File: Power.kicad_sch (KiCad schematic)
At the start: 26 parts, among them J2 Jack-DC, J6 Jack-DC, Q1 AO3401A, Q2 AO3401A, SW1 SW_SPDT_321, SW2 SW_SPDT_321, SW3 SW_SPDT_321, U1 XL4015

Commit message: Add DC Jack footprint
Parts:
- removed J2, J6: Jack-DC, symbol Connector:Jack-DC
- added J11, J6: Barrel_Jack_Switch, Connector_BarrelJack:BarrelJack_Kycon_KLDX-0202-xC_Horizontal, symbol Connector:Barrel_Jack_Switch
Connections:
- net +12V_DC_JACK: now also J6.1
- net GND: now also J11.2, J6.2
- net at SW2.2 (B): now also J11.1
- no-connect marks 0 -> 2
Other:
- moved on the sheet: C2, C6, D4, D5, Q1, Q2, R11, R12, R13, R14, R3, R4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

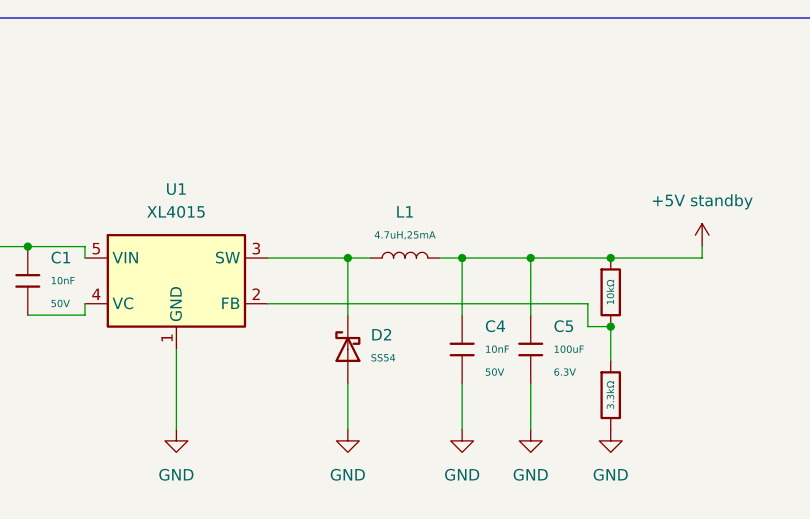
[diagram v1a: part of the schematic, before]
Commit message: Change inductor model
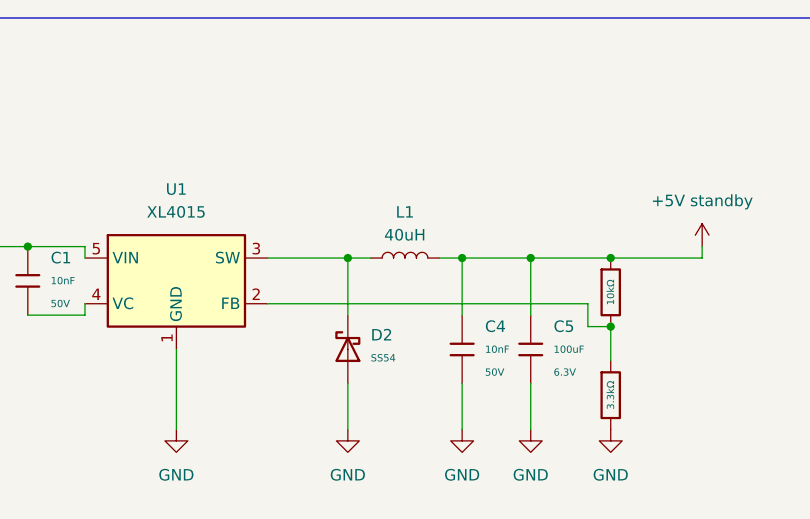
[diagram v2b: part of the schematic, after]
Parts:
- removed L1: 4.7uH,25mA, PCM_JLCPCB:L_1206, symbol PCM_JLCPCB-Inductors:4.7uH,25mA
- added L1: 40uH, Inductor_SMD:L_Bourns_SRR1260, symbol Device:L
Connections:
- net +5V standby: now also L1.2
- net at D2.1, U1.3 (SW): now also L1.1
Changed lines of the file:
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@@
-	)
-	(symbol
-		(lib_id "PCM_JLCPCB-Inductors:4.7uH,25mA")
-		(at 151.13 72.39 90)
-		(unit 1)
-		(exclude_from_sim no)
-		(in_bom yes)
-		(on_board yes)
-		(dnp no)
-		(fields_autoplaced yes)
-		(property "Reference" "L1"
-			(at 151.13 67.31 90)
-			(effects
-				(font
-					(size 1.27 1.27)
-				)
-			)
-		)
-		(property "Value" "4.7uH,25mA"
-			(at 151.13 69.85 90)
-			(effects
-				(font
-					(size 0.8 0.8)
-				)
-			)
-		)
-		(property "Footprint" "PCM_JLCPCB:L_1206"
-			(at 151.13 74.168 90)
-			(effects
-				(font
-					(size 1.27 1.27)
-				)
-				(hide yes)
-			)
-		)
-		(property "Datasheet" "https://www.lcsc.com/datasheet/lcsc_datasheet_2302231101_FH--Guangdong-Fenghua-Advanced-Tech-CMI321609U4R7KT_C1049.pdf"
-			(at 151.13 72.39 0)
-			(effects
-				(font
-					(size 1.27 1.27)
-				)
-				(hide yes)
-			)
-		)
-		(property "Description" "25mA 4.7uH ±10% 650mΩ 1206 Inductors (SMD) ROHS"
-			(at 151.13 72.39 0)
-			(effects
-				(font
-					(size 1.27 1.27)
-				)
-				(hide yes)
-			)
-		)
-		(property "LCSC" "C1049"
-			(at 151.13 72.39 0)
-			(effects
-				(font
-					(size 1.27 1.27)
-				)
-				(hide yes)
-			)
-		)
-		(property "Stock" "18027"
-			(at 151.13 72.39 0)
-			(effects
-				(font
-					(size 1.27 1.27)
-				)
-				(hide yes)
-			)
-		)
-		(property "Price" "0.019USD"
-			(at 151.13 72.39 0)
-			(effects
-				(font
-					(size 1.27 1.27)
-				)
-				(hide yes)
-			)
-		)
-		(property "Process" "SMT"
-			(at 151.13 72.39 0)
-			(effects
-				(font
-					(size 1.27 1.27)
-				)
-				(hide yes)
-			)
-		)
-		(property "Minimum Qty" "20"
-			(at 151.13 72.39 0)
-			(effects
-				(font
-					(size 1.27 1.27)
-				)
-				(hide yes)
-			)
-		)
-		(property "Attrition Qty" "10"
-			(at 151.13 72.39 0)
-			(effects
-				(font
-					(size 1.27 1.27)
-				)
-				(hide yes)
-			)
-		)
-		(property "Class" "Preferred Component"
-			(at 151.13 72.39 0)
-			(effects
-				(font
-					(size 1.27 1.27)
-				)
-				(hide yes)
-			)
-		)
-		(property "Category" "Inductors/Coils/Transformers,Inductors (SMD)"
-			(at 151.13 72.39 0)
-			(effects
-				(font
-					(size 1.27 1.27)
-				)
-				(hide yes)
-			)
-		)
-		(property "Manufacturer" "FH(Guangdong Fenghua Advanced Tech)"
-			(at 151.13 72.39 0)
-			(effects
-				(font
-					(size 1.27 1.27)
-				)
-				(hide yes)
-			)
-		)
-		(property "Part" "CMI321609U4R7KT"
-			(at 151.13 72.39 0)
-			(effects
-				(font
-					(size 1.27 1.27)
-				)
-				(hide yes)
-			)
-		)
-		(property "Inductance" "4.7uH"
-			(at 151.13 72.39 0)
-			(effects
-				(font
-					(size 1.27 1.27)
-				)
-				(hide yes)
-			)
-		)
-		(property "Q @ Freq" "35@10MHz"
-			(at 151.13 72.39 0)
-			(effects
-				(font
-					(size 1.27 1.27)
-				)
-				(hide yes)
-			)
-		)
-		(property "Frequency - Self Resonant" "35MHz"
-			(at 151.13 72.39 0)
-			(effects
-				(font
-					(size 1.27 1.27)
-				)
-				(hide yes)
-			)
-		)
-		(property "Tolerance" "±10%"
-			(at 151.13 72.39 0)
-			(effects
-				(font
-					(size 1.27 1.27)
-				)
-				(hide yes)
-			)
-		)
-		(property "Rated Current" "25mA"
-			(at 151.13 72.39 0)
-			(effects
-				(font
-					(size 1.27 1.27)
-				)
-				(hide yes)
-			)
-		)
-		(property "DC Resistance (DCR)" "650mΩ"
-			(at 151.13 72.39 0)
-			(effects
-				(font
-					(size 1.27 1.27)
-				)
-				(hide yes)
-			)
-		)
-		(pin "2"
-		)
-		(pin "1"
-		)
-		(instances
-			(project ""
-				(path "/31ac04e5-0b29-4cf4-90ae-9d7058f5ad37/ffc59f61-a8ed-4562-8b36-2c3c563e453a"
-					(reference "L1")
-					(unit 1)
-				)
-			)
-		)
 	)
 	(symbol
@@
 					(unit 1)
 				)
+			)
+		)
+	)
+	(symbol
+		(lib_id "Device:L")
+		(at 151.13 72.39 90)
+		(unit 1)
+		(exclude_from_sim no)
+		(in_bom yes)
+		(on_board yes)
+		(dnp no)
+		(fields_autoplaced yes)
+		(property "Reference" "L1"
+			(at 151.13 67.31 90)
+			(effects
+				(font
+					(size 1.27 1.27)
+				)
+			)
+		)
+		(property "Value" "40uH"
+			(at 151.13 69.85 90)
+			(effects
+				(font
+					(size 1.27 1.27)
+				)
+			)
+		)
+		(property "Footprint" "Inductor_SMD:L_Bourns_SRR1260"
+			(at 151.13 72.39 0)
+			(effects
+				(font
+					(size 1.27 1.27)
+				)
+				(hide yes)
+			)
+		)
+		(property "Datasheet" "~"
+			(at 151.13 72.39 0)
+			(effects
+				(font
+					(size 1.27 1.27)
+				)
+				(hide yes)
+			)
+		)
+		(property "Description" "Inductor"
+			(at 151.13 72.39 0)
+			(effects
+				(font
+					(size 1.27 1.27)
+				)
+				(hide yes)
+			)
+		)
+		(pin "2"
+		)
+		(pin "1"
+		)
+		(instances
+			(project "ModuCard-BreakoutBoard"
+				(path "/31ac04e5-0b29-4cf4-90ae-9d7058f5ad37/ffc59f61-a8ed-4562-8b36-2c3c563e453a"
+					(reference "L1")
+					(unit 1)
+				)

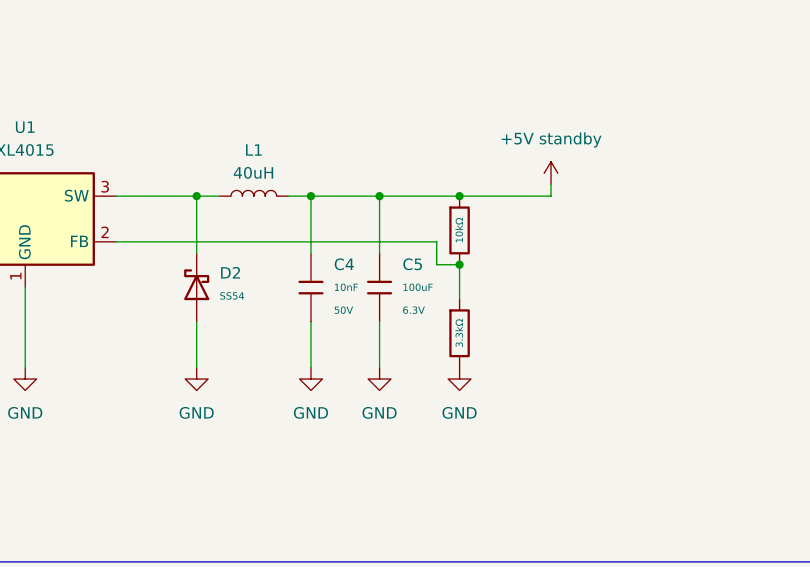
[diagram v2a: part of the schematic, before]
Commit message: Change capacitor
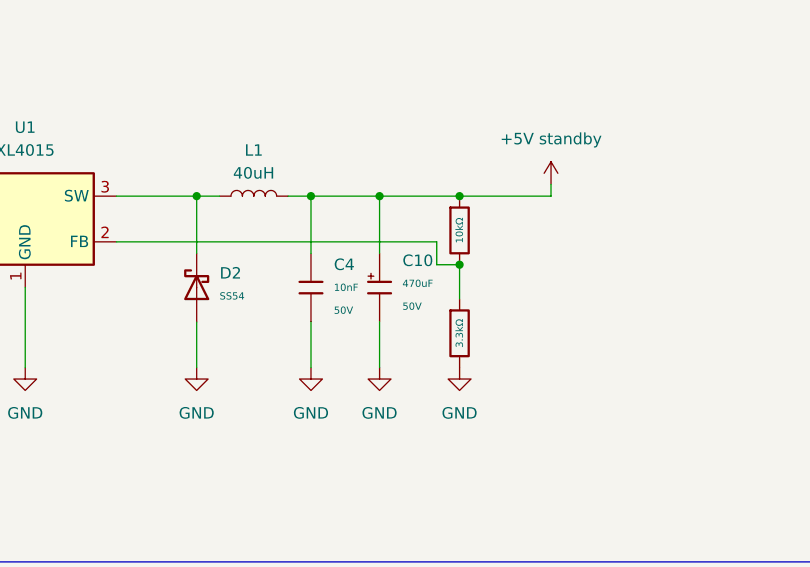
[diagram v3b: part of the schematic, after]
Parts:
- removed C5: 100uF, PCM_JLCPCB:C_1206, symbol PCM_JLCPCB-Capacitors:1206,100uF
- added C10: 470uF, PCM_JLCPCB:C_Plugin,D10xL16mm, symbol PCM_JLCPCB-Capacitors:Plugin,D10xL16mm,470uF
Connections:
- net +5V standby: now also C10.1
- net GND: now also C10.2
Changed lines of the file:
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@@
-	)
-	(symbol
-		(lib_id "PCM_JLCPCB-Capacitors:1206,100uF")
-		(at 165.1 82.55 0)
-		(unit 1)
-		(exclude_from_sim no)
-		(in_bom yes)
-		(on_board yes)
-		(dnp no)
-		(fields_autoplaced yes)
-		(property "Reference" "C5"
-			(at 167.64 80.0099 0)
-			(effects
-				(font
-					(size 1.27 1.27)
-				)
-				(justify left)
-			)
-		)
-		(property "Value" "100uF"
-			(at 167.64 82.55 0)
-			(effects
-				(font
-					(size 0.8 0.8)
-				)
-				(justify left)
-			)
-		)
-		(property "Footprint" "PCM_JLCPCB:C_1206"
-			(at 163.322 82.55 90)
-			(effects
-				(font
-					(size 1.27 1.27)
-				)
-				(hide yes)
-			)
-		)
-		(property "Datasheet" "https://www.lcsc.com/datasheet/lcsc_datasheet_2304140030_Samsung-Electro-Mechanics-CL31A107MQHNNNE_C15008.pdf"
-			(at 165.1 82.55 0)
-			(effects
-				(font
-					(size 1.27 1.27)
-				)
-				(hide yes)
-			)
-		)
-		(property "Description" "6.3V 100uF X5R ±20% 1206 Multilayer Ceramic Capacitors MLCC - SMD/SMT ROHS"
-			(at 165.1 82.55 0)
-			(effects
-				(font
-					(size 1.27 1.27)
-				)
-				(hide yes)
-			)
-		)
-		(property "LCSC" "C15008"
-			(at 165.1 82.55 0)
-			(effects
-				(font
-					(size 1.27 1.27)
-				)
-				(hide yes)
-			)
-		)
-		(property "Stock" "168402"
-			(at 165.1 82.55 0)
-			(effects
-				(font
-					(size 1.27 1.27)
-				)
-				(hide yes)
-			)
-		)
-		(property "Price" "0.063USD"
-			(at 165.1 82.55 0)
-			(effects
-				(font
-					(size 1.27 1.27)
-				)
-				(hide yes)
-			)
-		)
-		(property "Process" "SMT"
-			(at 165.1 82.55 0)
-			(effects
-				(font
-					(size 1.27 1.27)
-				)
-				(hide yes)
-			)
-		)
-		(property "Minimum Qty" "5"
-			(at 165.1 82.55 0)
-			(effects
-				(font
-					(size 1.27 1.27)
-				)
-				(hide yes)
-			)
-		)
-		(property "Attrition Qty" "4"
-			(at 165.1 82.55 0)
-			(effects
-				(font
-					(size 1.27 1.27)
-				)
-				(hide yes)
-			)
-		)
-		(property "Class" "Basic Component"
-			(at 165.1 82.55 0)
-			(effects
-				(font
-					(size 1.27 1.27)
-				)
-				(hide yes)
-			)
-		)
-		(property "Category" "Capacitors,Multilayer Ceramic Capacitors MLCC - SMD/SMT"
-			(at 165.1 82.55 0)
-			(effects
-				(font
-					(size 1.27 1.27)
-				)
-				(hide yes)
-			)
-		)
-		(property "Manufacturer" "Samsung Electro-Mechanics"
-			(at 165.1 82.55 0)
-			(effects
-				(font
-					(size 1.27 1.27)
-				)
-				(hide yes)
-			)
-		)
-		(property "Part" "CL31A107MQHNNNE"
-			(at 165.1 82.55 0)
-			(effects
-				(font
-					(size 1.27 1.27)
-				)
-				(hide yes)
-			)
-		)
-		(property "Voltage Rated" "6.3V"
-			(at 167.64 85.09 0)
-			(effects
-				(font
-					(size 0.8 0.8)
-				)
-				(justify left)
-			)
-		)
-		(property "Tolerance" "±20%"
-			(at 165.1 82.55 0)
-			(effects
-				(font
-					(size 1.27 1.27)
-				)
-				(hide yes)
-			)
-		)
-		(property "Capacitance" "100uF"
-			(at 165.1 82.55 0)
-			(effects
-				(font
-					(size 1.27 1.27)
-				)
-				(hide yes)
-			)
-		)
-		(property "Temperature Coefficient" "X5R"
-			(at 165.1 82.55 0)
-			(effects
-				(font
-					(size 1.27 1.27)
-				)
-				(hide yes)
-			)
-		)
-		(pin "1"
-		)
-		(pin "2"
-		)
-		(instances
-			(project ""
-				(path "/31ac04e5-0b29-4cf4-90ae-9d7058f5ad37/ffc59f61-a8ed-4562-8b36-2c3c563e453a"
-					(reference "C5")
-					(unit 1)
-				)
-			)
-		)
 	)
 	(symbol
@@
 					(unit 1)
 				)
+			)
+		)
+	)
+	(symbol
+		(lib_id "PCM_JLCPCB-Capacitors:Plugin,D10xL16mm,470uF")
+		(at 165.1 82.55 0)
+		(unit 1)
+		(exclude_from_sim no)
+		(in_bom yes)
+		(on_board yes)
+		(dnp no)
+		(fields_autoplaced yes)
+		(property "Reference" "C10"
+			(at 167.64 79.5654 0)
+			(effects
+				(font
+					(size 1.27 1.27)
+				)
+				(justify left)
+			)
+		)
+		(property "Value" "470uF"
+			(at 167.64 82.1055 0)
+			(effects
+				(font
+					(size 0.8 0.8)
+				)
+				(justify left)
+			)
+		)
+		(property "Footprint" "PCM_JLCPCB:C_Plugin,D10xL16mm"
+			(at 163.322 82.55 90)
+			(effects
+				(font
+					(size 1.27 1.27)
+				)
+				(hide yes)
+			)
+		)
+		(property "Datasheet" "https://wmsc.lcsc.com/wmsc/upload/file/pdf/v2/lcsc/2205131445_Man-Yue-Tech-EGT477M1HG16RRS0P_C3015599.pdf"
+			(at 165.1 82.55 0)
+			(effects
+				(font
+					(size 1.27 1.27)
+				)
+				(hide yes)
+			)
+		)
+		(property "Description" "470uF 50V ±20% Plugin,D10xL16mm Aluminum Electrolytic Capacitors - Leaded ROHS"
+			(at 165.1 82.55 0)
+			(effects
+				(font
+					(size 1.27 1.27)
+				)
+				(hide yes)
+			)
+		)
+		(property "LCSC" "C3015599"
+			(at 165.1 82.55 0)
+			(effects
+				(font
+					(size 1.27 1.27)
+				)
+				(hide yes)
+			)
+		)
+		(property "Stock" "2580"
+			(at 165.1 82.55 0)
+			(effects
+				(font
+					(size 1.27 1.27)
+				)
+				(hide yes)
+			)
+		)
+		(property "Price" "0.185USD"
+			(at 165.1 82.55 0)
+			(effects
+				(font
+					(size 1.27 1.27)
+				)
+				(hide yes)
+			)
+		)
+		(property "Process" "Hand-Soldered"
+			(at 165.1 82.55 0)
+			(effects
+				(font
+					(size 1.27 1.27)
+				)
+				(hide yes)
+			)
+		)
+		(property "Minimum Qty" "2"
+			(at 165.1 82.55 0)
+			(effects
+				(font
+					(size 1.27 1.27)
+				)
+				(hide yes)
+			)
+		)
+		(property "Attrition Qty" "0"
+			(at 165.1 82.55 0)
+			(effects
+				(font
+					(size 1.27 1.27)
+				)
+				(hide yes)
+			)
+		)
+		(property "Class" "Preferred Component"
+			(at 165.1 82.55 0)
+			(effects
+				(font
+					(size 1.27 1.27)
+				)
+				(hide yes)
+			)
+		)
+		(property "Category" "Capacitors,Aluminum Electrolytic Capacitors - Leaded"
+			(at 165.1 82.55 0)
+			(effects
+				(font
+					(size 1.27 1.27)
+				)
+				(hide yes)
+			)
+		)
+		(property "Manufacturer" "Man Yue Tech"
+			(at 165.1 82.55 0)
+			(effects
+				(font
+					(size 1.27 1.27)
+				)
+				(hide yes)
+			)
+		)
+		(property "Part" "EGT477M1HG16RRS0P"
+			(at 165.1 82.55 0)
+			(effects
+				(font
+					(size 1.27 1.27)
+				)
+				(hide yes)
+			)
+		)
+		(property "Voltage Rated" "50V"
+			(at 167.64 84.6455 0)
+			(effects
+				(font
+					(size 0.8 0.8)
+				)
+				(justify left)
+			)
+		)
+		(pin "2"
+		)
+		(pin "1"
+		)
+		(instances
+			(project ""
+				(path "/31ac04e5-0b29-4cf4-90ae-9d7058f5ad37/ffc59f61-a8ed-4562-8b36-2c3c563e453a"
+					(reference "C10")
+					(unit 1)
+				)
